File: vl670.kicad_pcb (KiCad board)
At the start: 4 copper layers, 60.3 x 22.4 mm, 72 parts, among them J1 Conn_01x07_Male, J2 USB_C_Receptacle, J3 Conn_01x07_Male, J4 USB3_A Receptacle, J5 Conn_01x02_Male, U1 HD3SS3220, U2 VL670, U3 4016, U4 TPS2061C-PXLI, U6 GD25D05, Y1 25MHz

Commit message: First private release.
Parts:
- removed C14, C15, C16, C17, C18: 1uF, Capacitor_SMD:C_0603_1608Metric_Pad1.08x0.95mm_HandSolder
- removed C23, C24: 330nF, Capacitor_SMD:C_0603_1608Metric
- removed JP3: SolderJumper_2_Bridged, Jumper:SolderJumper-2_P1.3mm_Bridged_RoundedPad1.0x1.5mm
- added C31: 470nF, Capacitor_SMD:C_0603_1608Metric_Pad1.08x0.95mm_HandSolder, B.Cu at (199.7, 122.7)
- added C32: 470nF, Capacitor_SMD:C_0603_1608Metric_Pad1.08x0.95mm_HandSolder, B.Cu at (204.1, 124.0)
- added C33: 470nF, Capacitor_SMD:C_0603_1608Metric_Pad1.08x0.95mm_HandSolder, B.Cu at (204.0, 120.7)
- added C34: 470nF, Capacitor_SMD:C_0603_1608Metric_Pad1.08x0.95mm_HandSolder, B.Cu at (201.2, 119.8)
- added C35: 470nF, Capacitor_SMD:C_0603_1608Metric_Pad1.08x0.95mm_HandSolder, B.Cu at (196.3, 124.8)
- added C41: 1uF, Capacitor_SMD:C_0603_1608Metric_Pad1.08x0.95mm_HandSolder, B.Cu at (201.2, 125.1)
- added C42: 1uF, Capacitor_SMD:C_0603_1608Metric_Pad1.08x0.95mm_HandSolder, B.Cu at (197.3, 126.4)
- added C43: 1uF, Capacitor_SMD:C_0603_1608Metric_Pad1.08x0.95mm_HandSolder, B.Cu at (199.7, 125.1)
- added C44: 1uF, Capacitor_SMD:C_0603_1608Metric_Pad1.08x0.95mm_HandSolder, F.Cu at (199.1, 117.5)
- added C51: 1uF, Capacitor_SMD:C_0603_1608Metric_Pad1.08x0.95mm_HandSolder, F.Cu at (195.6, 125.5)
- added C52: 1uF, Capacitor_SMD:C_0603_1608Metric_Pad1.08x0.95mm_HandSolder, B.Cu at (198.1, 121.2)
- added C61: 1uF, Capacitor_SMD:C_0603_1608Metric_Pad1.08x0.95mm_HandSolder, B.Cu at (203.9, 122.4)
- added C62: 1uF, Capacitor_SMD:C_0603_1608Metric_Pad1.08x0.95mm_HandSolder, B.Cu at (199.7, 118.8)
- added C71: 470nF, Capacitor_SMD:C_0402_1005Metric_Pad0.74x0.62mm_HandSolder, B.Cu at (206.1, 126.0)
- added C72: 470nF, Capacitor_SMD:C_0402_1005Metric_Pad0.74x0.62mm_HandSolder, B.Cu at (204.2, 126.0)
- added C73: 470nF, Capacitor_SMD:C_0402_1005Metric_Pad0.74x0.62mm_HandSolder, B.Cu at (185.8, 122.3)
- added C74: 470nF, Capacitor_SMD:C_0402_1005Metric_Pad0.74x0.62mm_HandSolder, B.Cu at (185.8, 126.0)
- added C75: 470nF, Capacitor_SMD:C_0402_1005Metric_Pad0.74x0.62mm_HandSolder, B.Cu at (202.3, 127.9)
- added C76: 470nF, Capacitor_SMD:C_0402_1005Metric_Pad0.74x0.62mm_HandSolder, B.Cu at (200.2, 127.9)
- added C77: 470nF, Capacitor_SMD:C_0402_1005Metric_Pad0.74x0.62mm_HandSolder, B.Cu at (191.3, 120.5)
- added C78: 470nF, Capacitor_SMD:C_0402_1005Metric_Pad0.74x0.62mm_HandSolder, B.Cu at (193.3, 120.5)
- added C79: 470nF, Capacitor_SMD:C_0402_1005Metric_Pad0.74x0.62mm_HandSolder, B.Cu at (177.2, 118.9)
- added C80: 470nF, Capacitor_SMD:C_0402_1005Metric_Pad0.74x0.62mm_HandSolder, B.Cu at (180.7, 118.9)
- added C81: 470nF, Capacitor_SMD:C_0402_1005Metric_Pad0.74x0.62mm_HandSolder, B.Cu at (177.2, 127.9)
- added C82: 470nF, Capacitor_SMD:C_0402_1005Metric_Pad0.74x0.62mm_HandSolder, B.Cu at (180.7, 127.9)
- added FID1: Fiducial, vl670:StencilFiducial_1mm, F.Cu at (173.7, 116.2)
- added FID2: Fiducial, vl670:StencilFiducial_0.5mm, F.Cu at (175.8, 117.0)
- added FID3: Fiducial, vl670:StencilFiducial_1mm, F.Cu at (230.9, 111.0)
- added FID4: Fiducial, vl670:StencilFiducial_0.5mm, F.Cu at (175.8, 129.4)
- added FID5: Fiducial, vl670:StencilFiducial_1mm, F.Cu at (173.7, 130.6)
- added FID6: Fiducial, vl670:StencilFiducial_0.5mm, F.Cu at (230.9, 113.3)
- added FID7: Fiducial, vl670:StencilFiducial_1mm, F.Cu at (230.9, 131.3)
- added FID8: Fiducial, vl670:StencilFiducial_0.5mm, F.Cu at (230.9, 129.0)
- added R15: 10k, Resistor_SMD:R_0603_1608Metric_Pad0.98x0.95mm_HandSolder, F.Cu at (213.6, 120.5)
- added R16: 100K, Resistor_SMD:R_0402_1005Metric_Pad0.72x0.64mm_HandSolder, F.Cu at (195.1, 131.3)
- added R17: 100K, Resistor_SMD:R_0402_1005Metric_Pad0.72x0.64mm_HandSolder, F.Cu at (195.1, 127.3)
- added R18: 1.8M, Resistor_SMD:R_0603_1608Metric_Pad0.98x0.95mm_HandSolder, F.Cu at (190.0, 128.8)
- added R19: 0R, Resistor_SMD:R_0603_1608Metric_Pad0.98x0.95mm_HandSolder, F.Cu at (195.6, 124.0)
- added U5: 74LVC2G66, Package_SO:VSSOP-8_2.4x2.1mm_P0.5mm, F.Cu at (208.0, 116.0)
- C1, C3, C4, C5, C6, C7: value 1uF -> 220nF; moved to F.Cu
- C2: value 1uF -> 230nF; moved to F.Cu
- C22, C25, C26, C9: value 1uF -> 470nF
- C8: value 1uF -> 220nF
- D10, D11, D12, D13, D15, D16, D17, D18, D8, D9: value D_TVS -> ESD7951S; footprint Diode_SMD:D_SOD-923 -> Diode_SMD:D_SOD-523
- D14, D7: footprint Diode_SMD:D_SOD-923 -> Diode_SMD:D_SOD-523
- J2: footprint Connector_USB:USB_C_Receptacle_Amphenol_12401548E4-2A -> vl670:USB_C_Receptacle_XKB_U262-241N-4BV60
- J4: footprint Connector_USB:USB3_A_Molex_48393-001 -> vl670:USB3_A_Receptacle_Wuerth_692112030100_Horizontal
- JP1, R5, R6, R7, R8, R9: moved to B.Cu
- L1: footprint Inductor_SMD:L_0603_1608Metric_Pad1.05x0.95mm_HandSolder -> Inductor_SMD:L_1008_2520Metric_Pad1.43x2.20mm_HandSolder
- R10: value 10K -> 10k
- R11: value 10K -> 10k; moved to B.Cu
- R12: value 900k -> 1.8M
- U3: value 4016 -> 74LVC2G66; footprint Package_SO:TSSOP-14_4.4x5mm_P0.65mm -> Package_SO:VSSOP-8_2.4x2.1mm_P0.5mm; moved to F.Cu
- moved C22 32.8 mm to (202.4, 112.0), turned to 90 degrees
- moved C3 21.0 mm to (185.4, 128.8), turned to 270 degrees
- moved R4 19.8 mm to (200.4, 111.4)
- moved C4 19.6 mm to (183.9, 128.8)
- moved C1 19.3 mm to (183.9, 118.6)
- moved U6 18.1 mm to (209.8, 117.7), turned to 180 degrees
- moved U3 18.1 mm to (212.5, 116.0)
- moved C26 17.6 mm to (205.0, 116.5), turned to 270 degrees
- moved C13 17.2 mm to (200.4, 113.0), turned to 180 degrees
- moved C2 14.9 mm to (185.4, 118.6)
- moved R10 14.6 mm to (215.6, 117.2), turned to 180 degrees
- moved R5 12.6 mm to (198.2, 128.9), turned to 270 degrees
- moved D2 12.5 mm to (190.2, 116.8)
- moved JP2 11.9 mm to (183.8, 118.6), turned to 90 degrees
- moved R11 11.8 mm to (215.6, 119.0)
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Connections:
- net /D+ renamed /D_DEMUX+
- net /D- renamed /D_DEMUX-
- net /USB MUX/ESD/CC1 renamed /USB AC CAP/ESD/MUX/CC1
- net /USB MUX/ESD/CC2 renamed /USB AC CAP/ESD/MUX/CC2
- net /USB MUX/ESD/D+ renamed /USB AC CAP/ESD/MUX/D+
- net /USB MUX/ESD/D- renamed /USB AC CAP/ESD/MUX/D-
- net /USB MUX/ESD/RX2+ renamed /USB AC CAP/ESD/MUX/RX2+
- net /USB MUX/ESD/RX2- renamed /USB AC CAP/ESD/MUX/RX2-
- C1 pad 1: +3V3 -> /USB AC CAP/ESD/MUX/TX1_AC-
- C1 pad 2: GND -> /USB AC CAP/ESD/MUX/TX1-
- C13 pad 1: Net-(C13-Pad1) -> ~EXT_RESET
- C2 pad 1: +3V3 -> /USB AC CAP/ESD/MUX/TX1_AC+
- C2 pad 2: GND -> /USB AC CAP/ESD/MUX/TX1+
- C3 pad 1: +3V3 -> /USB AC CAP/ESD/MUX/TX2_AC-
- C3 pad 2: GND -> /USB AC CAP/ESD/MUX/TX2+
- C4 pad 1: +3V3 -> /USB AC CAP/ESD/MUX/TX2_AC+
- C4 pad 2: GND -> /USB AC CAP/ESD/MUX/TX2-
- C5 pad 1: +3V3 -> /SSTX_DEMUX-
- C5 pad 2: GND -> /USB AC CAP/ESD/MUX/TX_MUX_DC-
- C6 pad 1: +1V5 -> /SSTX_DEMUX+
- C6 pad 2: GND -> /USB AC CAP/ESD/MUX/TX_MUX_DC+
- C7 pad 1: +1V5 -> /DN_TX_AC-
- C7 pad 2: GND -> /DN_SSTX-
- C8 pad 1: +1V5 -> /DN_TX_AC+
- C8 pad 2: GND -> /DN_SSTX+
- C9 pad 1: +1V5 -> +3V3
- D1 pad 1: /USB MUX/ESD/RX1- -> /USB AC CAP/ESD/MUX/RX1+
- D1 pad 10: /USB MUX/ESD/RX1- -> /USB AC CAP/ESD/MUX/RX1+
- D1 pad 2: /USB MUX/ESD/RX1+ -> /USB AC CAP/ESD/MUX/RX1-
- D1 pad 4: /USB MUX/ESD/TX1+ -> /USB AC CAP/ESD/MUX/TX1+
- D1 pad 5: /USB MUX/ESD/TX1- -> /USB AC CAP/ESD/MUX/TX1-
- D1 pad 6: /USB MUX/ESD/TX1- -> /USB AC CAP/ESD/MUX/TX1-
- D1 pad 7: /USB MUX/ESD/TX1+ -> /USB AC CAP/ESD/MUX/TX1+
- D1 pad 9: /USB MUX/ESD/RX1+ -> /USB AC CAP/ESD/MUX/RX1-
- D17 pad 1: /eeprom/~ISP_ENABLE -> ~EXT_RESET
- D3 pad 1: /DN_USB3RX- -> +5V_SW
- D3 pad 10: /DN_USB3RX- -> +5V_SW
- D3 pad 2: /DN_USB3RX+ -> +5V_SW
- D3 pad 4: +5V_SW -> /DN_D-
- D3 pad 5: +5V_SW -> /DN_D+
- D3 pad 6: +5V_SW -> /DN_D+
- D3 pad 7: +5V_SW -> /DN_D-
- D3 pad 9: /DN_USB3RX+ -> +5V_SW
- D4 pad 4: /USB MUX/ESD/TX2+ -> /USB AC CAP/ESD/MUX/TX2-
- D4 pad 5: /USB MUX/ESD/TX2- -> /USB AC CAP/ESD/MUX/TX2+
- D4 pad 6: /USB MUX/ESD/TX2- -> /USB AC CAP/ESD/MUX/TX2+
- D4 pad 7: /USB MUX/ESD/TX2+ -> /USB AC CAP/ESD/MUX/TX2-
- D6 pad 1: /DN_USB3TX- -> /DN_TX_AC-
- D6 pad 10: /DN_USB3TX- -> /DN_TX_AC-
- D6 pad 2: /DN_USB3TX+ -> /DN_TX_AC+
- D6 pad 4: /DN_D- -> /DN_SSRX-
- D6 pad 5: /DN_D+ -> /DN_SSRX+
- D6 pad 6: /DN_D+ -> /DN_SSRX+
- D6 pad 7: /DN_D- -> /DN_SSRX-
- D6 pad 9: /DN_USB3TX+ -> /DN_TX_AC+
- J1 pad 6: /eeprom/~ISP_ENABLE -> ~EXT_RESET
- J2 pad A2: /USB MUX/ESD/TX1+ -> /USB AC CAP/ESD/MUX/TX1+
- J2 pad A3: /USB MUX/ESD/TX1- -> /USB AC CAP/ESD/MUX/TX1-
- J2 pad B10: /USB MUX/ESD/RX1- -> /USB AC CAP/ESD/MUX/RX1-
- J2 pad B11: /USB MUX/ESD/RX1+ -> /USB AC CAP/ESD/MUX/RX1+
- J2 pad B2: /USB MUX/ESD/TX2+ -> /USB AC CAP/ESD/MUX/TX2+
- J2 pad B3: /USB MUX/ESD/TX2- -> /USB AC CAP/ESD/MUX/TX2-
- J4 pad 5: /DN_USB3RX- -> /DN_SSRX-
- J4 pad 6: /DN_USB3RX+ -> /DN_SSRX+
- J4 pad 8: /DN_USB3TX- -> /DN_TX_AC+
- J4 pad 9: /DN_USB3TX+ -> /DN_TX_AC-
- R3 pad 2: /eeprom/~ISP_ENABLE -> ~EXT_RESET
- R4 pad 2: Net-(C13-Pad1) -> ~EXT_RESET
- U1 pad 10: /USB MUX/ESD/RX+ -> /SSRX_DEMUX+
- U1 pad 14: /USB MUX/ESD/RX1- -> /USB AC CAP/ESD/MUX/RX1+
- U1 pad 15: /USB MUX/ESD/RX1+ -> /USB AC CAP/ESD/MUX/RX1-
- U1 pad 16: /USB MUX/ESD/TX1+ -> /USB AC CAP/ESD/MUX/TX1_AC+
- U1 pad 17: /USB MUX/ESD/TX1- -> /USB AC CAP/ESD/MUX/TX1_AC-
- U1 pad 20: /USB MUX/ESD/TX2+ -> /USB AC CAP/ESD/MUX/TX2_AC+
- U1 pad 21: /USB MUX/ESD/TX2- -> /USB AC CAP/ESD/MUX/TX2_AC-
- U1 pad 6: /USB MUX/ESD/TX- -> /USB AC CAP/ESD/MUX/TX_MUX_DC-
- U1 pad 7: /USB MUX/ESD/TX+ -> /USB AC CAP/ESD/MUX/TX_MUX_DC+
- U1 pad 9: /USB MUX/ESD/RX- -> /SSRX_DEMUX-
- U2 pad 13: /TX+ -> /SSTX_DEMUX+
- U2 pad 14: /TX- -> /SSTX_DEMUX-
- U2 pad 16: /DN_USB3RX- -> /DN_SSRX-
- U2 pad 17: /DN_USB3RX+ -> /DN_SSRX+
- U2 pad 18: /USB MUX/ESD/RX+ -> /SSRX_DEMUX-
- U2 pad 19: /USB MUX/ESD/RX- -> /SSRX_DEMUX+
- U2 pad 21: /DN_USB3TX- -> /DN_SSTX-
- U2 pad 22: /DN_USB3TX+ -> /DN_SSTX+
- U2 pad 34: Net-(C13-Pad1) -> ~EXT_RESET
- U2 pad 8: GND -> Net-(R19-Pad1)
- U3 pad 3: /eeprom/ISP_SCK -> ~EXT_RESET
- U3 pad 4: /eeprom/SCK -> GND
- U3 pad 5: /eeprom/~ISP_ENABLE -> /eeprom/SCK
- U3 pad 6: /eeprom/~ISP_ENABLE -> /eeprom/ISP_SCK
- U3 pad 7: GND -> ~EXT_RESET
- U3 pad 8: /eeprom/MOSI -> +3V3
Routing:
- net /DN_SSRX-: track 0.00 -> 78.7 mm
- net /DN_SSRX+: track 0.00 -> 76.7 mm
- net /DN_TX_AC-: track 0.00 -> 71.4 mm
- net /DN_TX_AC+: track 0.00 -> 69.5 mm
- net ~EXT_RESET: track 0.00 -> 50.9 mm, vias 0 -> 5
- net /eeprom/~ISP_ENABLE: track 33.4 -> 0.00 mm, vias 3 -> 0
- net Net-(D9-Pad1): track 66.6 -> 36.8 mm, vias 3 -> 1
- net /eeprom/MOSI: track 42.4 -> 13.2 mm, vias 3 -> 0
- net /USB AC CAP/ESD/MUX/RX1-: track 0.00 -> 28.9 mm, vias 0 -> 1
- net /DN_USB3TX+: track 28.7 -> 0.00 mm, vias 2 -> 0
- net /DN_USB3TX-: track 28.7 -> 0.00 mm, vias 2 -> 0
- net /D_DEMUX+: track 10.1 -> 38.7 mm, vias 0 -> 2
- net /USB AC CAP/ESD/MUX/RX1+: track 0.00 -> 28.5 mm, vias 0 -> 1
- net /D_DEMUX-: track 8.69 -> 37.1 mm, vias 0 -> 2
- net /eeprom/MISO: track 36.6 -> 9.62 mm, vias 1 -> 0
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- added copper zone on B.Cu, net +1V5
- added copper zone on F.Cu, net +1V5
- removed copper zone on B.Cu, net GND
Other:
- board size 60.3 x 22.4 mm -> 64.9 x 25.1 mm
- board text added: "IO1"
- board text added: "IO2"
- board text added: "IO3"
- board text added: "IO4"
- board text added: "RX"
- board text added: "TX"
- board text removed: "G1"
- board text removed: "G2"
- board text removed: "G3"
- board text removed: "G4"
- board text removed: "U1"
- board text removed: "U2"

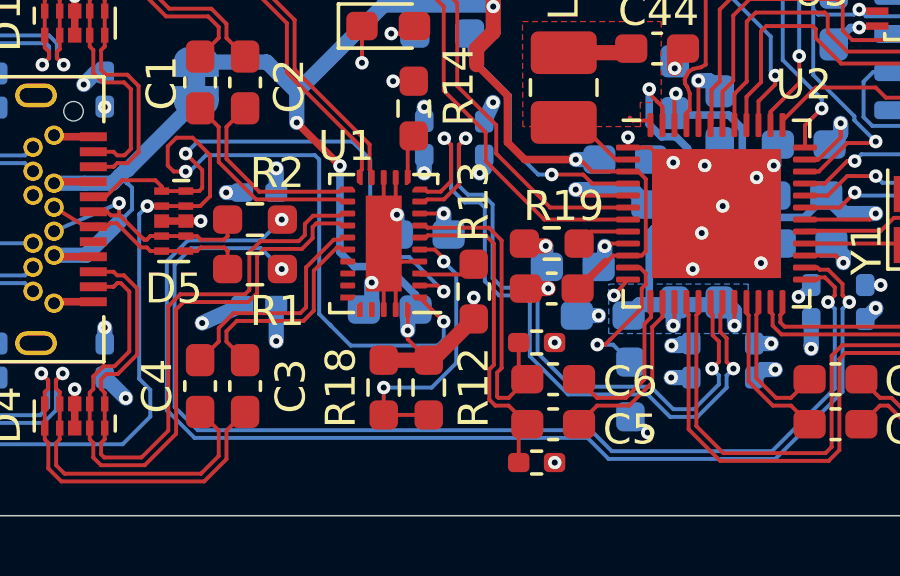
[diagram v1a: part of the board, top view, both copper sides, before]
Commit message: Change R13 to a no-connection item
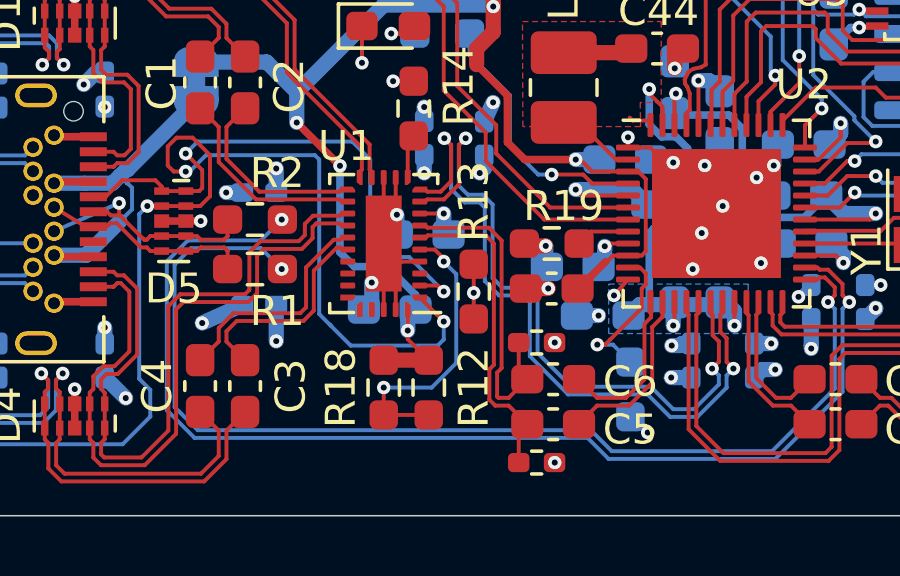
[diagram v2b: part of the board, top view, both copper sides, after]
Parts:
- C2: value 230nF -> 220nF
- R13: value 500k -> NC
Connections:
- R13 pad 1: Net-(R13-Pad1) -> GND
- R13 pad 2: +5V -> GND
- U1 pad 3: Net-(R13-Pad1) -> Net-(U1-Pad3)
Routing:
- net +5V: track 107.5 -> 104.9 mm, vias 10 -> 9
- net GND: track 78.0 -> 80.3 mm, vias 63 -> 64
- net Net-(R13-Pad1): track 1.95 -> 0.00 mm

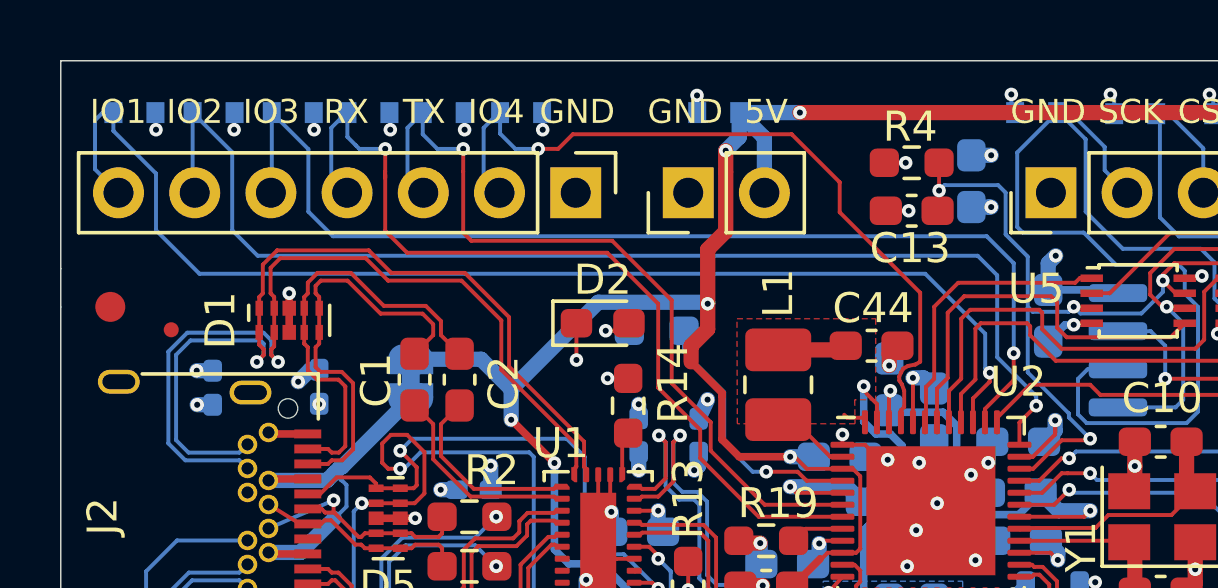
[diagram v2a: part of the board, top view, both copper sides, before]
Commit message: Change GPIO connections to match firmware.
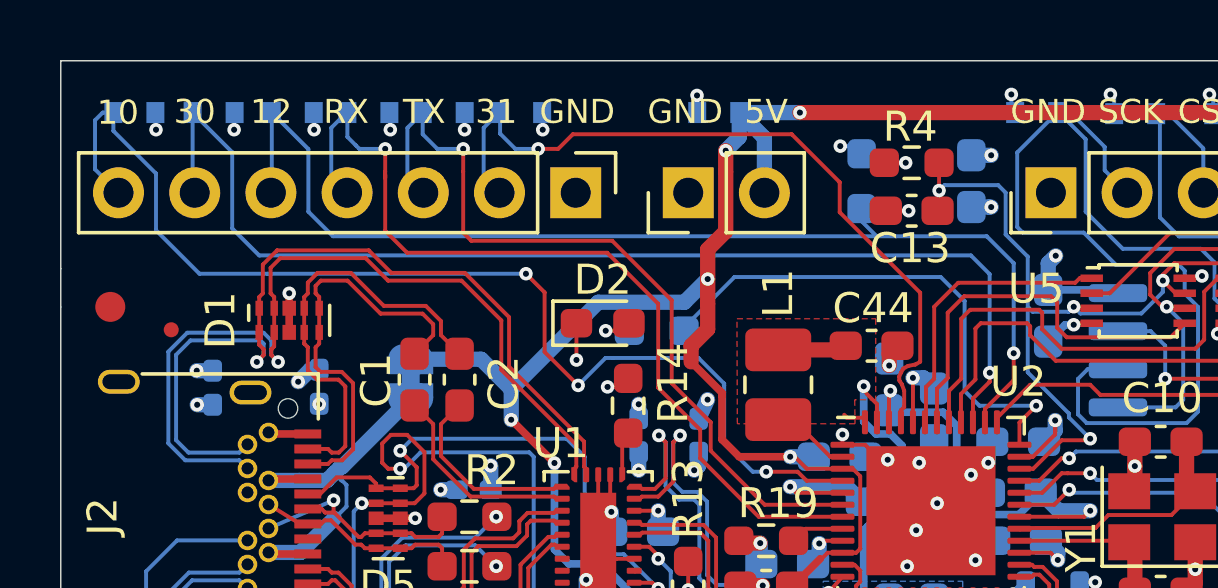
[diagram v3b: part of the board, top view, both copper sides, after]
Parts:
- added R20: 10k, Resistor_SMD:R_0603_1608Metric_Pad0.98x0.95mm_HandSolder, B.Cu at (198.8, 112.0)
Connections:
- U2 pad 36: Net-(D8-Pad1) -> Net-(R9-Pad2)
- U2 pad 39: Net-(D7-Pad1) -> Net-(D8-Pad1)
- U2 pad 4: Net-(R9-Pad2) -> Net-(D7-Pad1)
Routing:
- net Net-(R9-Pad2): track 8.82 -> 17.7 mm
- net Net-(D7-Pad1): track 40.8 -> 37.9 mm, vias 1 -> 3
- net Net-(D8-Pad1): track 40.0 -> 38.6 mm
- net Net-(D9-Pad1): track 36.8 -> 38.0 mm
- net GND: track 80.3 -> 81.2 mm, vias 64 -> 65
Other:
- board text added: "10"
- board text added: "12"
- board text added: "30"
- board text added: "31"
- board text removed: "IO1"
- board text removed: "IO2"
- board text removed: "IO3"
- board text removed: "IO4"

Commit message: various changes for v0.01 public release.
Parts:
- added G***: LOGO, vl670:lain, B.Cu at (229.7, 122.1)
- added R21: 10k, Resistor_SMD:R_0603_1608Metric_Pad0.98x0.95mm_HandSolder, B.Cu at (198.6, 111.5)
- C7, C8: value 220nF -> 100nF
- moved R20 1.46 mm to (200.2, 111.5)
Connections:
- C3 pad 1: /USB AC CAP/ESD/MUX/TX2_AC- -> /USB AC CAP/ESD/MUX/TX2_AC+
- C4 pad 1: /USB AC CAP/ESD/MUX/TX2_AC+ -> /USB AC CAP/ESD/MUX/TX2_AC-
- U1 pad 20: /USB AC CAP/ESD/MUX/TX2_AC+ -> /USB AC CAP/ESD/MUX/TX2_AC-
- U1 pad 21: /USB AC CAP/ESD/MUX/TX2_AC- -> /USB AC CAP/ESD/MUX/TX2_AC+
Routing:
- net GND: track 81.2 -> 85.5 mm, vias 65 -> 64
- net Net-(D8-Pad1): track 38.6 -> 41.3 mm
- net Net-(D9-Pad1): track 38.0 -> 40.2 mm
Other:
- board text added: "Let's all love Lain"

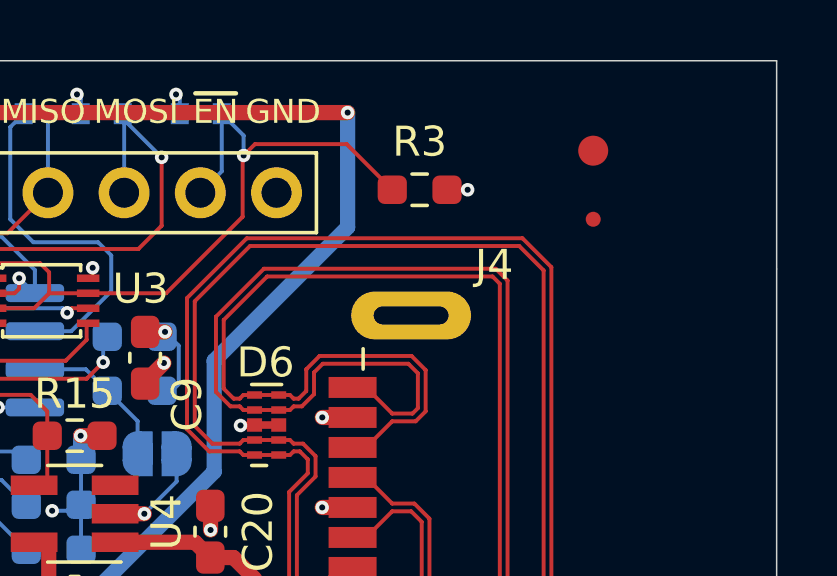
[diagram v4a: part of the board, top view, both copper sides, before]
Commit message: rename components and footprints.
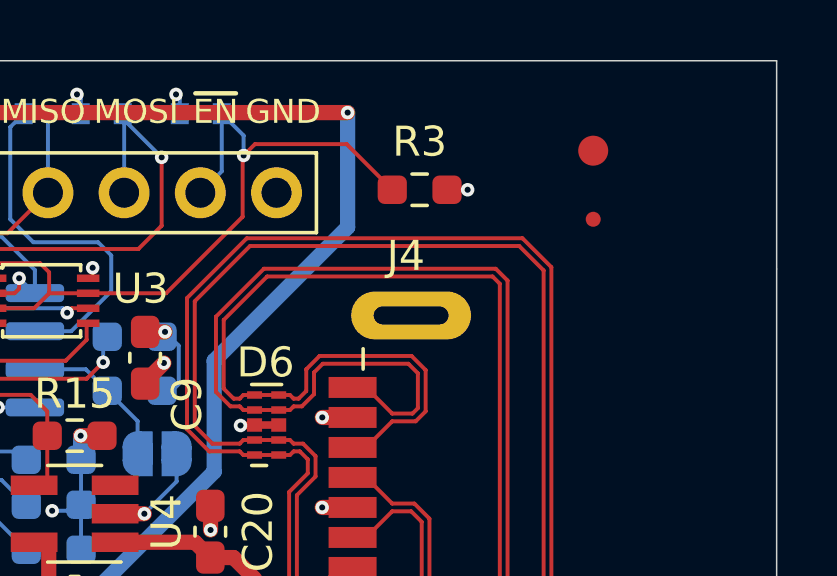
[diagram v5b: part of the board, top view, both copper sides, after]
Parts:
- D14, D7: value ESD7951S -> ESD5B5.0ST1G-N
- J4: footprint vl670:USB3_A_Receptacle_Wuerth_692112030100_Horizontal -> vl670:USB3_A_Receptacle_XKB_U231-091N-4BLRA00-S-1

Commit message: v0.02.
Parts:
- added D19: ESD7951S, Diode_SMD:D_SOD-523, B.Cu at (174.3, 109.7)
- added D20: LED, LED_SMD:LED_0603_1608Metric_Pad1.05x0.95mm_HandSolder, F.Cu at (219.7, 123.7)
- added FB1: Ferrite_Bead_Small, Inductor_SMD:L_0603_1608Metric_Pad1.05x0.95mm_HandSolder, B.Cu at (183.0, 119.6)
- added H1: MountingHole_Pad, MountingHole:MountingHole_2.5mm_Pad_Via, F.Cu at (175.0, 106.0)
- added H2: MountingHole_Pad, MountingHole:MountingHole_2.5mm_Pad_Via, F.Cu at (175.0, 135.0)
- added H3: MountingHole_Pad, MountingHole:MountingHole_2.5mm_Pad_Via, F.Cu at (234.0, 106.0)
- added H4: MountingHole_Pad, MountingHole:MountingHole_2.5mm_Pad_Via, F.Cu at (234.0, 135.0)
- added R22: 0R5, Resistor_SMD:R_0603_1608Metric_Pad0.98x0.95mm_HandSolder, F.Cu at (217.2, 125.7)
- added R23: 0R5, Resistor_SMD:R_0603_1608Metric_Pad0.98x0.95mm_HandSolder, B.Cu at (216.7, 127.2)
- added R24: 470R, Resistor_SMD:R_0603_1608Metric_Pad0.98x0.95mm_HandSolder, F.Cu at (229.3, 112.3)
- added TP1: TestPoint, TestPoint:TestPoint_Pad_D1.0mm, F.Cu at (188.0, 131.8)
- added TP2: TestPoint, TestPoint:TestPoint_Pad_D1.0mm, F.Cu at (196.0, 115.4)
- added TP3: TestPoint, TestPoint:TestPoint_Pad_D1.0mm, F.Cu at (199.4, 131.8)
- C10, C11: value 20pF -> 18pF
- C19: value 1uF -> 10uF
- C20: value 1uF -> 10uF; moved to B.Cu
- C7, C8: value 100nF -> 220nF
- J3: value Conn_01x07_Male -> Conn_01x08_Male; footprint Connector_PinHeader_2.54mm:PinHeader_1x07_P2.54mm_Vertical -> Connector_PinHeader_2.54mm:PinHeader_1x08_P2.54mm_Vertical
- R13: value NC -> 470R; moved to B.Cu
- moved J3 15.3 mm to (174.0, 112.4), turned to 90 degrees
- moved R13 9.06 mm to (188.2, 117.9)
- moved FID8 4.27 mm to (233.9, 126.0)
- moved FID7 3.61 mm to (233.9, 129.3)
- moved C20 3.50 mm to (218.2, 127.2), turned to 270 degrees
- moved R21 3.16 mm to (201.5, 112.9), turned to 0 degrees
- moved FID6 3.08 mm to (233.9, 114.0)
- moved FID3 3.00 mm to (233.9, 111.0)
- moved J5 2.46 mm to (195.5, 112.4)
- moved C22 2.46 mm to (201.5, 109.8), turned to 0 degrees
- moved D10 2.40 mm to (184.7, 109.7)
- moved D11 2.40 mm to (187.2, 109.7)
- moved D12 2.40 mm to (189.8, 109.7)
- moved D7 2.40 mm to (176.9, 109.7)
- moved D8 2.40 mm to (179.6, 109.7)
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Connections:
- C19 pad 2: GND -> Net-(C19-Pad2)
- C20 pad 2: GND -> Net-(C20-Pad2)
- FID1 pad : (no net) -> GND
- FID2 pad : (no net) -> GND
- FID3 pad : (no net) -> GND
- FID4 pad : (no net) -> GND
- FID5 pad : (no net) -> GND
- FID6 pad : (no net) -> GND
- FID7 pad : (no net) -> GND
- FID8 pad : (no net) -> GND
- J3 pad 1: GND -> Net-(D19-Pad1)
- J3 pad 2: Net-(D12-Pad1) -> Net-(D7-Pad1)
- J3 pad 3: Net-(D11-Pad1) -> Net-(D8-Pad1)
- J3 pad 4: Net-(D10-Pad1) -> Net-(D9-Pad1)
- J3 pad 5: Net-(D9-Pad1) -> Net-(D10-Pad1)
- J3 pad 6: Net-(D8-Pad1) -> Net-(D11-Pad1)
- J3 pad 7: Net-(D7-Pad1) -> Net-(D12-Pad1)
- J5 pad 1: GND -> +5V
- J5 pad 2: +5V -> GND
- JP2 pad 1: +5VP -> Net-(FB1-Pad1)
- R13 pad 1: GND -> Net-(D2-Pad2)
- R13 pad 2: GND -> Net-(D19-Pad1)
- R9 pad 2: Net-(R9-Pad2) -> Net-(D7-Pad1)
- U2 pad 36: Net-(R9-Pad2) -> Net-(D7-Pad1)
- U2 pad 4: Net-(D7-Pad1) -> Net-(D19-Pad1)
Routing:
- net GND: track 85.5 -> 686.8 mm, vias 64 -> 172
- net Net-(D19-Pad1): track 0.00 -> 38.7 mm, vias 0 -> 3
- net Net-(R9-Pad2): track 17.7 -> 0.00 mm, vias 1 -> 0
- net Net-(D20-Pad1): track 0.00 -> 17.4 mm, vias 0 -> 2
- net +1V2: track 15.1 -> 32.3 mm, vias 2 -> 3
- net +5V: track 105.1 -> 112.7 mm, vias 9 -> 12
- net Net-(D7-Pad1): track 37.9 -> 43.5 mm, vias 3 -> 1
- net +1V5: track 21.3 -> 25.4 mm
- net Net-(D8-Pad1): track 41.3 -> 38.3 mm
- net Net-(D2-Pad2): track 1.67 -> 4.43 mm
- net Net-(D10-Pad1): track 30.0 -> 27.4 mm
- net Net-(D11-Pad1): track 27.1 -> 24.5 mm
- net Net-(FB1-Pad1): track 0.00 -> 2.25 mm
- net Net-(D12-Pad1): track 26.5 -> 24.3 mm, vias 1 -> 3
- net +3V3: track 35.2 -> 37.4 mm
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- added copper zone on B.Cu, net +5V
- added copper zone on F.Cu, net +5V
- added copper zone on B.Cu, net GND
- added copper zone on F.Cu, net GND
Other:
- board size 64.9 x 25.1 mm -> 65 x 35 mm
- board text added: "1.0"
- board text added: "1.1"
- board text added: "1.2"
- board text added: "3.0"
- board text added: "3.1"
- board text added: "VL670"
- board text added: "VL671"
- board text removed: "10"
- board text removed: "12"
- board text removed: "30"
- board text removed: "31"
